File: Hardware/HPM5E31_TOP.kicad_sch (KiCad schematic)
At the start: 19 parts, among them J1 Conn_Coaxial, J2 Conn_Coaxial, J3 WAFER-ZH1.5-4PWB, J4 Conn_02x05_Odd_Even, K1 DSHP02TSGET

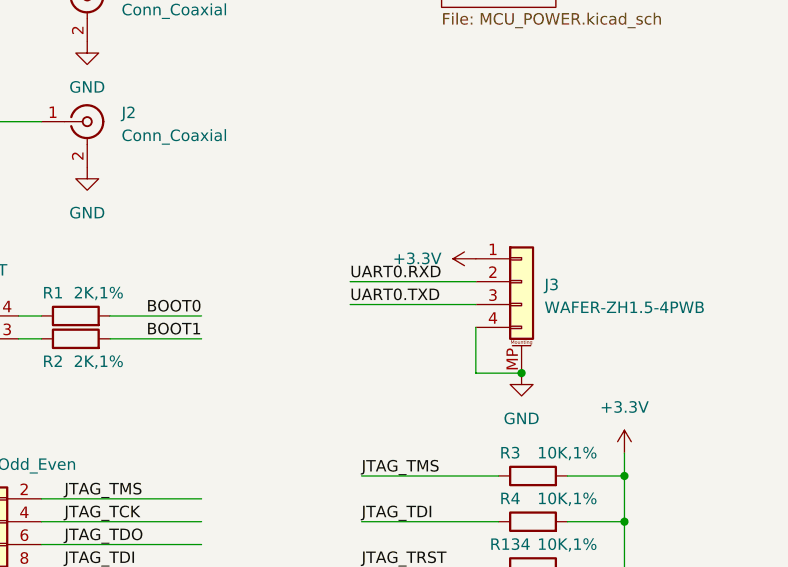
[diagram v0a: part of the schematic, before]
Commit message: 修改PCB，上传py32抱闸驱动代码，上传HPM board
调整抱闸驱动栅极电阻
急停光耦增加上拉电阻和滤波电路
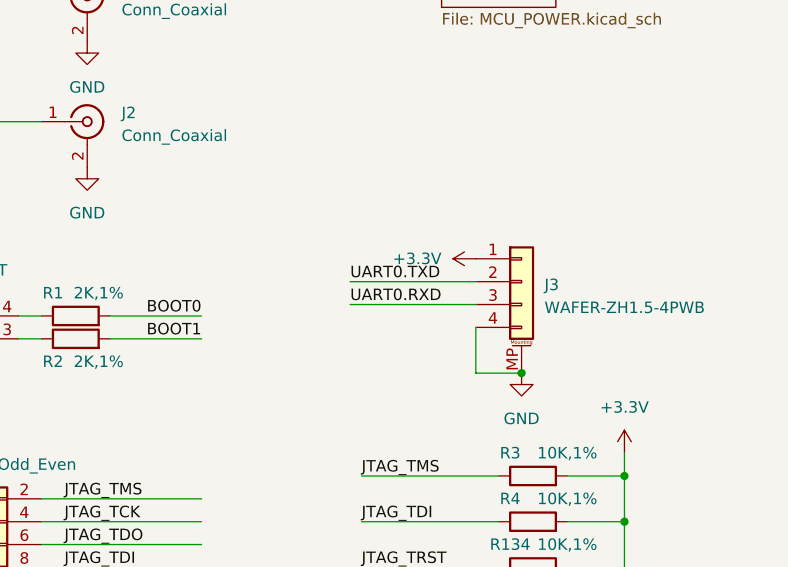
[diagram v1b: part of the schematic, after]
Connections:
- net PA0: now also J3.3 (Pin_3); no longer J3.2 (Pin_2)
- net PA1: now also J3.2 (Pin_2); no longer J3.3 (Pin_3)
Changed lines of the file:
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@@
 	)
 	(label "UART0.RXD"
-		(at 240.03 106.68 0)
+		(at 240.03 109.22 0)
 		(effects
 			(font
@@
 	)
 	(label "UART0.TXD"
-		(at 240.03 109.22 0)
+		(at 240.03 106.68 0)
 		(effects
 			(font

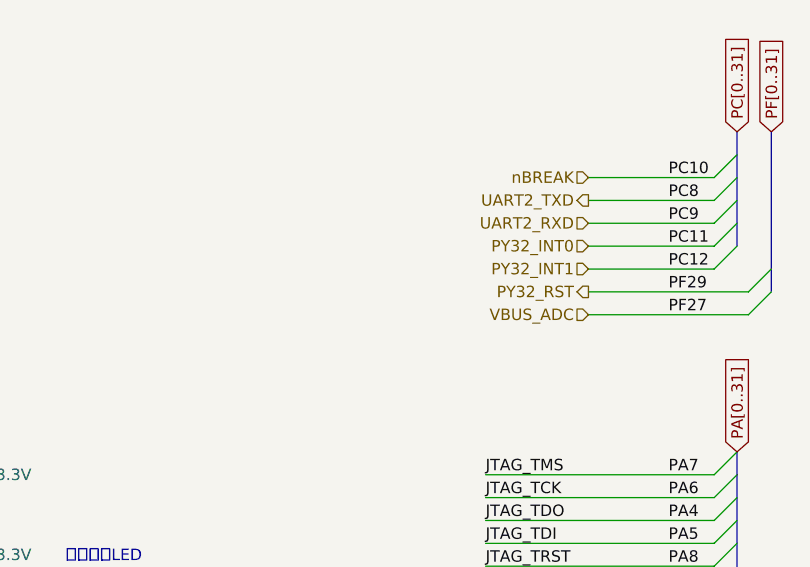
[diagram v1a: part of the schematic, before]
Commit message: PCB和foc_demo
PCB：
部分信号增加测试点
半桥增加栅极电容和RC吸收（待定），泄放mos是否需要栅极电容待测
软件：
增加foc_demo半成品
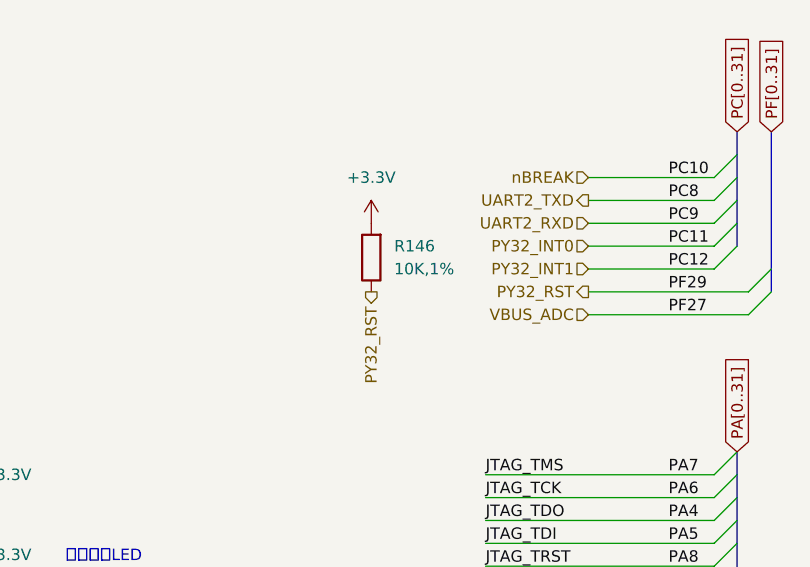
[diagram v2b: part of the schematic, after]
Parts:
- added R146: 10K,1%, Resistor_SMD:R_0402_1005Metric, symbol HPM6280Foc:0402WGF1002TCE
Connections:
- net +3.3V: now also R146.2
- net PY32_RST: now also R146.1
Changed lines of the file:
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@@
+		)
+	)
+	(hierarchical_label "PY32_RST"
+		(shape output)
+		(at 116.84 148.59 270)
+		(effects
+			(font
+				(size 1.27 1.27)
+			)
+			(justify right)
 		)
 	)
@@
 	(symbol
 		(lib_id "power:+3.3V")
+		(at 116.84 140.97 0)
+		(unit 1)
+		(exclude_from_sim no)
+		(in_bom yes)
+		(on_board yes)
+		(dnp no)
+		(fields_autoplaced yes)
+		(property "Reference" "#PWR0352"
+			(at 116.84 144.78 0)
+			(effects
+				(font
+					(size 1.27 1.27)
+				)
+				(hide yes)
+			)
+		)
+		(property "Value" "+3.3V"
+			(at 116.84 135.89 0)
+			(effects
+				(font
+					(size 1.27 1.27)
+				)
+			)
+		)
+		(property "Footprint" ""
+			(at 116.84 140.97 0)
+			(effects
+				(font
+					(size 1.27 1.27)
+				)
+				(hide yes)
+			)
+		)
+		(property "Datasheet" ""
+			(at 116.84 140.97 0)
+			(effects
+				(font
+					(size 1.27 1.27)
+				)
+				(hide yes)
+			)
+		)
+		(property "Description" "Power symbol creates a global label with name \"+3.3V\""
+			(at 116.84 140.97 0)
+			(effects
+				(font
+					(size 1.27 1.27)
+				)
+				(hide yes)
+			)
+		)
+		(pin "1"
+		)
+		(instances
+			(project "HPM5E31_ECatDualFOC"
+				(path "/a07e9810-3899-4327-ba8f-f24142a7c70e/b9a8d5a3-7d25-4818-87f6-adc719379948"
+					(reference "#PWR0352")
+					(unit 1)
+				)
+			)
+		)
+	)
+	(symbol
+		(lib_id "power:+3.3V")
 		(at 254 104.14 90)
 		(unit 1)
@@
 					(unit 1)
 				)
+			)
+		)
+	)
+	(symbol
+		(lib_id "HPM6280Foc:0402WGF1002TCE")
+		(at 116.84 144.78 90)
+		(unit 1)
+		(exclude_from_sim no)
+		(in_bom yes)
+		(on_board yes)
+		(dnp no)
+		(fields_autoplaced yes)
+		(property "Reference" "R146"
+			(at 119.38 143.5099 90)
+			(effects
+				(font
+					(size 1.27 1.27)
+				)
+				(justify right)
+			)
+		)
+		(property "Value" "10K,1%"
+			(at 119.38 146.0499 90)
+			(effects
+				(font
+					(size 1.27 1.27)
+				)
+				(justify right)
+			)
+		)
+		(property "Footprint" "Resistor_SMD:R_0402_1005Metric"
+			(at 116.84 144.78 0)
+			(effects
+				(font
+					(size 1.27 1.27)
+				)
+				(hide yes)
+			)
+		)
+		(property "Datasheet" "https://atta.szlcsc.com/upload/public/pdf/source/20200306/C422600_1E6D84923E4A46A82E41ADD87F860B5C.pdf"
+			(at 116.84 144.78 0)
+			(effects
+				(font
+					(size 1.27 1.27)
+				)
+				(hide yes)
+			)
+		)
+		(property "Description" ""
+			(at 116.84 144.78 0)
+			(effects
+				(font
+					(size 1.27 1.27)
+				)
+				(hide yes)
+			)
+		)
+		(property "华秋编号" "G0063278"
+			(at 116.84 144.78 0)
+			(effects
+				(font
+					(size 1.27 1.27)
+				)
+				(hide yes)
+			)
+		)
+		(property "立创编号" "C25744"
+			(at 116.84 144.78 0)
+			(effects
+				(font
+					(size 1.27 1.27)
+				)
+				(hide yes)
+			)
+		)
+		(pin "2"
+		)
+		(pin "1"
+		)
+		(instances
+			(project ""
+				(path "/a07e9810-3899-4327-ba8f-f24142a7c70e/b9a8d5a3-7d25-4818-87f6-adc719379948"
+					(reference "R146")
+					(unit 1)
+				)

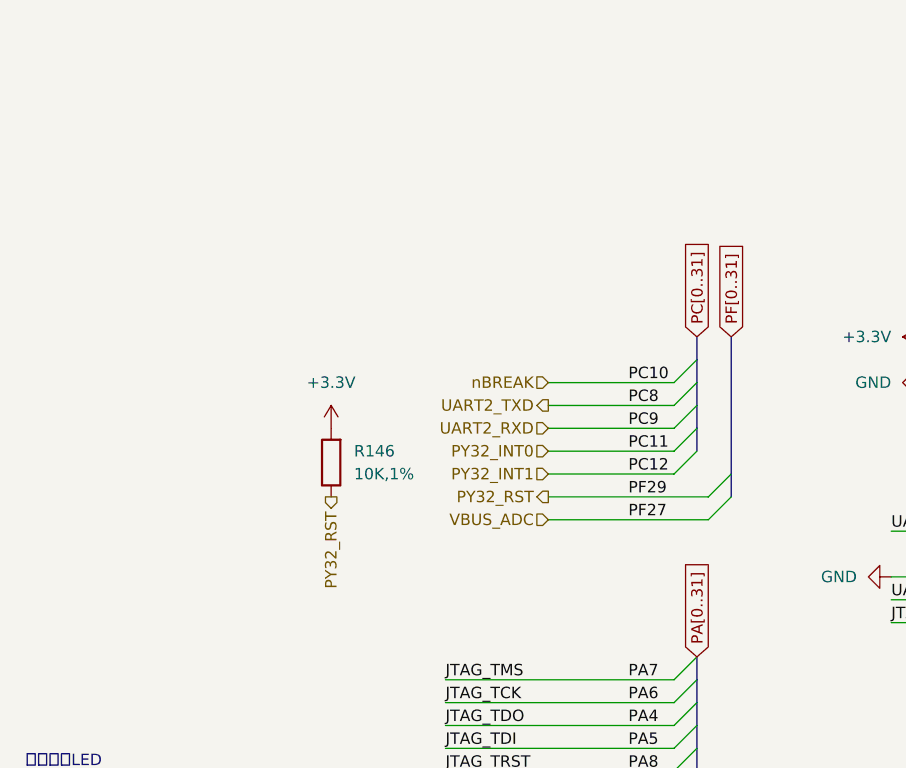
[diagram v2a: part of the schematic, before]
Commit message: PCB：风扇增加控制IO，泄放驱动增加使能引脚，485编码器电源接入控制
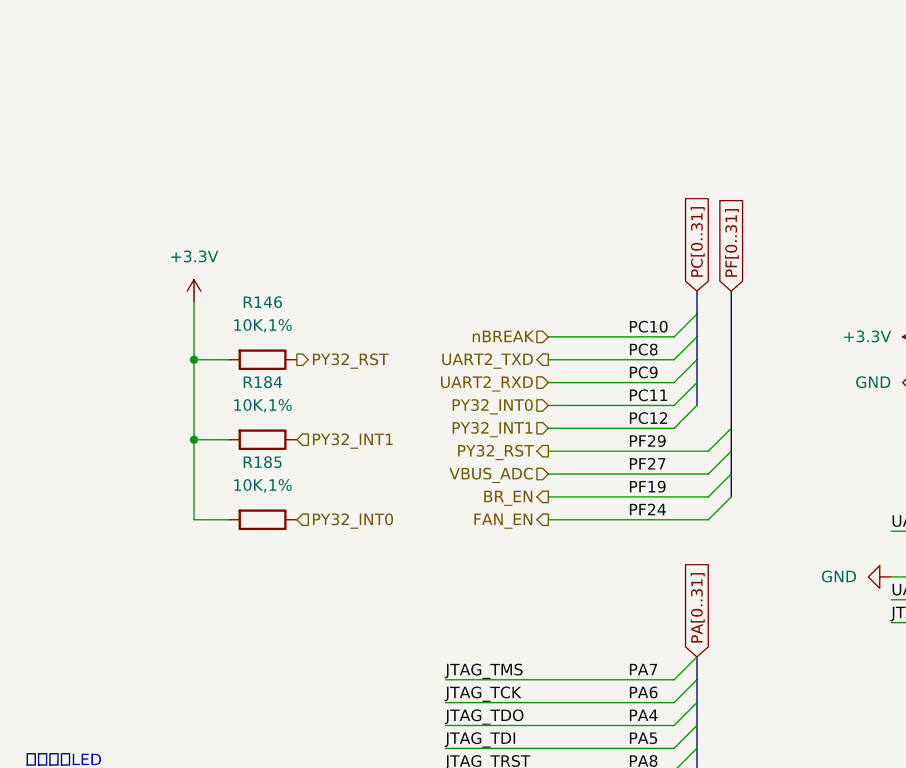
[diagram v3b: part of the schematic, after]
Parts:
- added R184, R185: 10K,1%, Resistor_SMD:R_0402_1005Metric, symbol HPM6280Foc:0402WGF1002TCE
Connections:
- net +3.3V: now also R184.2, R185.2
- net PY32_INT0: now also R185.1
- net PY32_INT1: now also R184.1
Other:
- moved on the sheet: R146
